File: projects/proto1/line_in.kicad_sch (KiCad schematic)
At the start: 16 parts, among them U55 MC33078

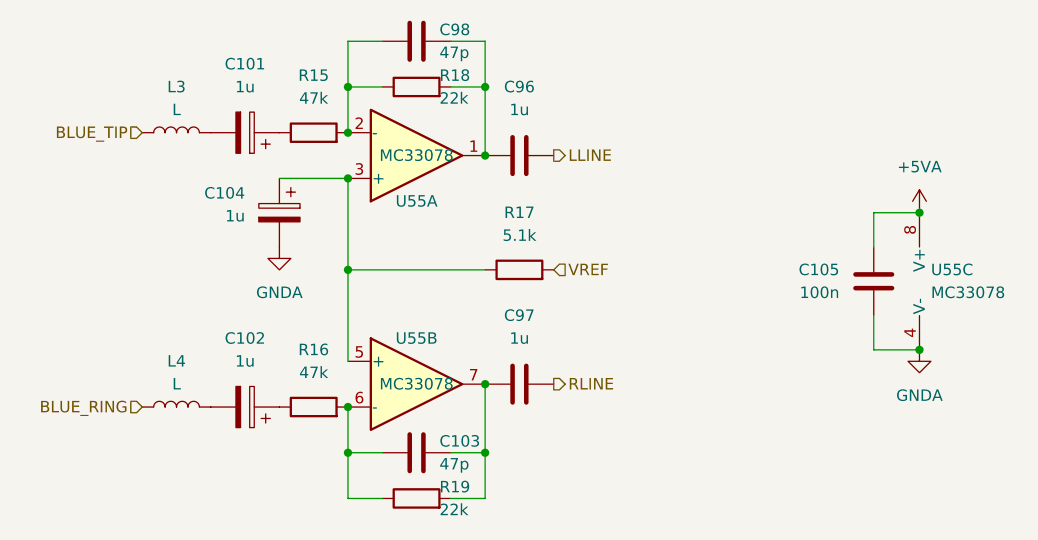
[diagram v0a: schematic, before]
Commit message: Renamed CMC to SCU, changed verification method to cocotb, and modified pcb schematic
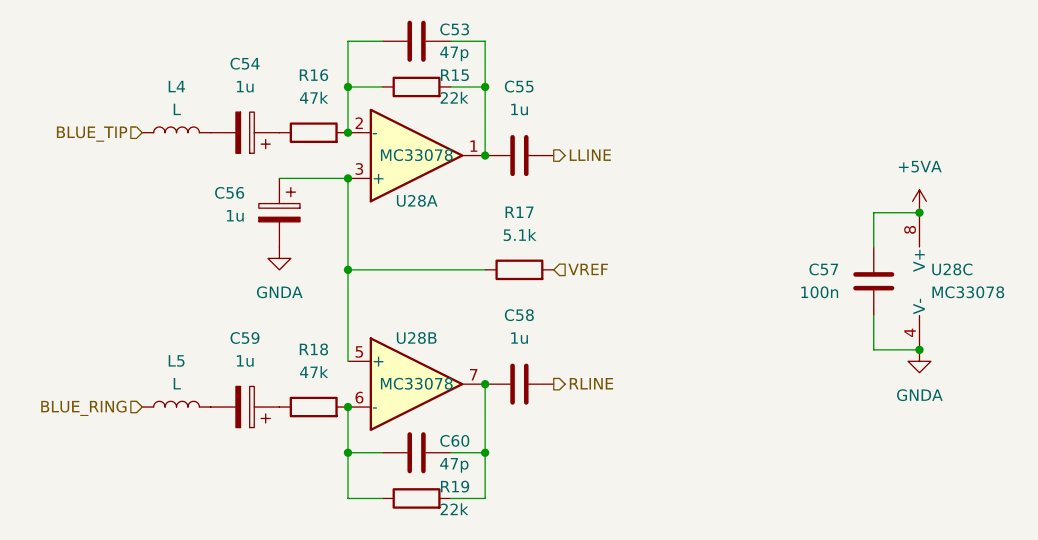
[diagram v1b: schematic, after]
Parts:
- renumbered C98 to C53, C101 to C54, C96 to C55, C104 to C56, C105 to C57, C97 to C58, C102 to C59, C103 to C60, L3 to L4, L4 to L5, R18 to R15, R15 to R16, R16 to R18, U55 to U28
